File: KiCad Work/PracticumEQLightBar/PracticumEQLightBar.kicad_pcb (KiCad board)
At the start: 2 copper layers, 20 parts, among them U1 TEENSY 4.1, U2 TEENSY AUDIO ADAPTER BOARD RE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

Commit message: Updates to LED layout to match 49 key on schematic and PCB
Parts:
- removed the D8 at (104.8, 57.3)
- removed the D8 at (24.3, 57.4)
- removed the D8 at (137.0, 57.3)
- removed the D8 at (40.3, 57.3)
- removed the D8 at (72.7, 57.4)
- removed the D8 at (88.8, 57.3)
- removed the D8 at (121.0, 57.4)
- removed the D8 at (56.3, 57.3)
- removed the D8 at (153.0, 57.3)
- removed the D9 at (64.7, 57.5)
- removed the D9 at (129.0, 57.4)
- removed the D9 at (112.9, 57.5)
- removed the D9 at (48.3, 57.3)
- removed the D9 at (145.0, 57.3)
- removed the D9 at (16.2, 57.5)
- removed the D9 at (96.8, 57.3)
- removed the D9 at (32.3, 57.4)
- removed the D9 at (80.8, 57.4)
- added D1: APA102, LED_SMD:LED_RGB_5050-6, F.Cu at (61.0, 99.1)
- added D10: APA102, LED_SMD:LED_RGB_5050-6, F.Cu at (141.0, 99.1)
- added D11: APA102, LED_SMD:LED_RGB_5050-6, F.Cu at (149.9, 99.1)
- added D12: APA102, LED_SMD:LED_RGB_5050-6, F.Cu at (158.8, 99.1)
- added D13: APA102, LED_SMD:LED_RGB_5050-6, F.Cu at (167.6, 99.1)
- added D14: APA102, LED_SMD:LED_RGB_5050-6, F.Cu at (176.5, 99.1)
- added D15: APA102, LED_SMD:LED_RGB_5050-6, F.Cu at (185.4, 99.1)
- added D16: APA102, LED_SMD:LED_RGB_5050-6, F.Cu at (194.3, 99.1)
- added D17: APA102, LED_SMD:LED_RGB_5050-6, F.Cu at (203.2, 99.1)
- added D18: APA102, LED_SMD:LED_RGB_5050-6, F.Cu at (212.1, 99.1)
- added D19: APA102, LED_SMD:LED_RGB_5050-6, F.Cu at (221.0, 99.1)
- added D2: APA102, LED_SMD:LED_RGB_5050-6, F.Cu at (69.8, 99.1)
- added D20: APA102, LED_SMD:LED_RGB_5050-6, F.Cu at (229.9, 99.1)
- added D21: APA102, LED_SMD:LED_RGB_5050-6, F.Cu at (238.8, 99.1)
- added D22: APA102, LED_SMD:LED_RGB_5050-6, F.Cu at (247.7, 99.1)
- added D23: APA102, LED_SMD:LED_RGB_5050-6, F.Cu at (256.5, 99.1)
- added D24: APA102, LED_SMD:LED_RGB_5050-6, F.Cu at (265.4, 99.1)
- added D25: APA102, LED_SMD:LED_RGB_5050-6, F.Cu at (274.3, 99.1)
- added D26: APA102, LED_SMD:LED_RGB_5050-6, F.Cu at (283.2, 99.1)
- added D27: APA102, LED_SMD:LED_RGB_5050-6, F.Cu at (292.1, 99.1)
- added D28: APA102, LED_SMD:LED_RGB_5050-6, F.Cu at (301.0, 99.1)
- added D29: APA102, LED_SMD:LED_RGB_5050-6, F.Cu at (309.9, 99.1)
- added D3: APA102, LED_SMD:LED_RGB_5050-6, F.Cu at (78.7, 99.1)
- added D30: APA102, LED_SMD:LED_RGB_5050-6, F.Cu at (295.9, 90.2)
- added D31: APA102, LED_SMD:LED_RGB_5050-6, F.Cu at (287.0, 90.2)
- added D32: APA102, LED_SMD:LED_RGB_5050-6, F.Cu at (278.1, 90.2)
- added D33: APA102, LED_SMD:LED_RGB_5050-6, F.Cu at (260.4, 90.2)
- added D34: APA102, LED_SMD:LED_RGB_5050-6, F.Cu at (251.5, 90.2)
- added D35: APA102, LED_SMD:LED_RGB_5050-6, F.Cu at (233.7, 90.2)
- added D36: APA102, LED_SMD:LED_RGB_5050-6, F.Cu at (224.8, 90.2)
- added D37: APA102, LED_SMD:LED_RGB_5050-6, F.Cu at (215.9, 90.2)
- added D38: APA102, LED_SMD:LED_RGB_5050-6, F.Cu at (198.1, 90.2)
- added D39: APA102, LED_SMD:LED_RGB_5050-6, F.Cu at (189.2, 90.2)
- added D4: APA102, LED_SMD:LED_RGB_5050-6, F.Cu at (87.6, 99.1)
- added D40: APA102, LED_SMD:LED_RGB_5050-6, F.Cu at (171.4, 90.2)
- added D41: APA102, LED_SMD:LED_RGB_5050-6, F.Cu at (162.6, 90.2)
- added D42: APA102, LED_SMD:LED_RGB_5050-6, F.Cu at (153.7, 90.2)
- added D43: APA102, LED_SMD:LED_RGB_5050-6, F.Cu at (135.9, 90.2)
- added D44: APA102, LED_SMD:LED_RGB_5050-6, F.Cu at (127.0, 90.2)
- added D45: APA102, LED_SMD:LED_RGB_5050-6, F.Cu at (109.2, 90.2)
- added D46: APA102, LED_SMD:LED_RGB_5050-6, F.Cu at (100.3, 90.2)
- added D47: APA102, LED_SMD:LED_RGB_5050-6, F.Cu at (91.4, 90.2)
- added D48: APA102, LED_SMD:LED_RGB_5050-6, F.Cu at (73.7, 90.2)
- added D49: APA102, LED_SMD:LED_RGB_5050-6, F.Cu at (64.8, 90.2)
- added D5: APA102, LED_SMD:LED_RGB_5050-6, F.Cu at (96.5, 99.1)
- added D6: APA102, LED_SMD:LED_RGB_5050-6, F.Cu at (105.4, 99.1)
- added D7: APA102, LED_SMD:LED_RGB_5050-6, F.Cu at (114.3, 99.1)
- added D8: APA102, LED_SMD:LED_RGB_5050-6, F.Cu at (123.2, 99.1)
- added D9: APA102, LED_SMD:LED_RGB_5050-6, F.Cu at (132.1, 99.1)
- moved U1 106.9 mm to (68.6, 205.7)
- moved U2 48.2 mm to (111.8, 208.3)
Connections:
- U1 pad GND1: Net-(D8-GND) -> unconnected-(U1-GND-PadGND1)
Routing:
- net Net-(D1-VCC): track 0.00 -> 806.5 mm
- net Net-(D1-DI): track 0.00 -> 92.0 mm
- net Net-(D1-CI): track 0.00 -> 85.2 mm
- net Net-(D29-CO): track 0.00 -> 25.7 mm
- net Net-(D29-DO): track 0.00 -> 19.5 mm
- net Net-(D42-DO): track 0.00 -> 13.0 mm
- net Net-(D42-CO): track 0.00 -> 13.0 mm
- net Net-(D39-DO): track 0.00 -> 13.0 mm
- net Net-(D39-CO): track 0.00 -> 13.0 mm
- net Net-(D32-DO): track 0.00 -> 13.0 mm
- net Net-(D32-CO): track 0.00 -> 13.0 mm
- net Net-(D47-DO): track 0.00 -> 13.0 mm
- net Net-(D47-CO): track 0.00 -> 13.0 mm
- net Net-(D44-DO): track 0.00 -> 13.0 mm
- net Net-(D44-CO): track 0.00 -> 13.0 mm
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- added copper zone on B.Cu, net (none)
- added copper zone on F.Cu, net (none)
- added copper zone on B.Cu, net GND
- added copper zone on F.Cu, net GND
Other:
- board outline added: 300 x 300 mm

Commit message: Completed preliminary schematic
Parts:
- moved U2 48.2 mm to (66.0, 192.9), turned to -90 degrees
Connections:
- D1 pad 1: Net-(D1-DI) -> unconnected-(D1-DI-Pad1)
- D1 pad 2: Net-(D1-CI) -> unconnected-(D1-CI-Pad2)
- D45 pad 1: Net-(D44-DO) -> Net-(D45-DI)
- D45 pad 2: Net-(D44-CO) -> Net-(D45-CI)
- D7 pad 5: Net-(D7-CO) -> Net-(D45-CI)
- D7 pad 6: Net-(D7-DO) -> Net-(D45-DI)
- U1 pad 0: Net-(D1-CI) -> Net-(U1-RX1)
- U1 pad 1: Net-(D1-DI) -> Net-(U1-TX1)
- U1 pad 10: unconnected-(U1-CS1-Pad10) -> Net-(U1-CS1)
- U1 pad 11: unconnected-(U1-MOSI-Pad11) -> Net-(U1-MOSI)
- U1 pad 12: unconnected-(U1-MISO-Pad12) -> Net-(U1-MISO)
- U1 pad 13: unconnected-(U1-SCK-Pad13) -> Net-(U1-SCK)
- U1 pad 14: unconnected-(U1-A0-Pad14) -> Net-(U1-A0)
- U1 pad 15: unconnected-(U1-A1-Pad15) -> Net-(U1-A1)
- U1 pad 16: unconnected-(U1-A2-Pad16) -> Net-(U1-A2)
- U1 pad 17: unconnected-(U1-A3-Pad17) -> Net-(U1-A3)
- U1 pad 18: unconnected-(U1-A4-Pad18) -> Net-(U1-A4)
- U1 pad 19: unconnected-(U1-A5-Pad19) -> Net-(U1-A5)
- U1 pad 2: unconnected-(U1-OUT2-Pad2) -> Net-(U1-OUT2)
- U1 pad 20: unconnected-(U1-A6-Pad20) -> Net-(U1-A6)
- U1 pad 21: unconnected-(U1-A7-Pad21) -> Net-(U1-A7)
- U1 pad 22: unconnected-(U1-A8-Pad22) -> Net-(U1-A8)
- U1 pad 23: unconnected-(U1-A9-Pad23) -> Net-(U1-A9)
- U1 pad 3: unconnected-(U1-LRCLK2-Pad3) -> Net-(U1-LRCLK2)
- U1 pad 3.3V_2: unconnected-(U1-3.3V__1-Pad3.3V_2) -> Net-(U1-3.3V__1)
- U1 pad 4: unconnected-(U1-BCLK2-Pad4) -> Net-(U1-BCLK2)
- U1 pad 5: unconnected-(U1-IN2-Pad5) -> Net-(U1-IN2)
- U1 pad 5V: Net-(D1-VCC) -> unconnected-(U1-Pad5V)
- U1 pad 6: unconnected-(U1-OUT1D-Pad6) -> Net-(U1-OUT1D)
- U1 pad 7: unconnected-(U1-RX2-Pad7) -> Net-(U1-RX2)
- U1 pad 8: unconnected-(U1-TX2-Pad8) -> Net-(U1-TX2)
- U1 pad 9: unconnected-(U1-OUT1C-Pad9) -> Net-(U1-OUT1C)
- U1 pad GND1: unconnected-(U1-GND-PadGND1) -> Net-(U1-GND)
- U1 pad GND3: unconnected-(U1-GND__2-PadGND3) -> Net-(U1-GND__2)
- U1 pad VIN: unconnected-(U1-PadVIN) -> Net-(U1-PadVIN)
- U2 pad 0: unconnected-(U2-Pad0) -> Net-(U1-RX1)
- U2 pad 1: unconnected-(U2-Pad1) -> Net-(U1-TX1)
- U2 pad 10: unconnected-(U2-SDCS-Pad10) -> Net-(U1-CS1)
- U2 pad 11: unconnected-(U2-MOSI-Pad11) -> Net-(U1-MOSI)
- U2 pad 12: unconnected-(U2-MISO-Pad12) -> Net-(U1-MISO)
- U2 pad 13: unconnected-(U2-SCK-Pad13) -> Net-(U1-SCK)
- U2 pad 14: unconnected-(U2-Pad14) -> Net-(U1-A0)
- U2 pad 15: unconnected-(U2-VOL15_A1-Pad15) -> Net-(U1-A1)
- U2 pad 16: unconnected-(U2-Pad16) -> Net-(U1-A2)
- U2 pad 17: unconnected-(U2-Pad17) -> Net-(U1-A3)
- U2 pad 18: unconnected-(U2-SDA-Pad18) -> Net-(U1-A4)
- U2 pad 19: unconnected-(U2-SCL-Pad19) -> Net-(U1-A5)
- U2 pad 2: unconnected-(U2-Pad2) -> Net-(U1-OUT2)
- U2 pad 20: unconnected-(U2-LRCLK1-Pad20) -> Net-(U1-A6)
- U2 pad 21: unconnected-(U2-BCLK1-Pad21) -> Net-(U1-A7)
- U2 pad 22: unconnected-(U2-Pad22) -> Net-(U1-A8)
- U2 pad 23: unconnected-(U2-MCLK1-Pad23) -> Net-(U1-A9)
- U2 pad 3: unconnected-(U2-Pad3) -> Net-(U1-LRCLK2)
- U2 pad 3V: unconnected-(U2-Pad3V) -> Net-(U1-3.3V__1)
- U2 pad 4: unconnected-(U2-Pad4) -> Net-(U1-BCLK2)
- U2 pad 5: unconnected-(U2-Pad5) -> Net-(U1-IN2)
- U2 pad 5V: unconnected-(U2-Pad5V) -> Net-(U1-PadVIN)
- U2 pad 6: unconnected-(U2-MEMCS-Pad6) -> Net-(U1-OUT1D)
- U2 pad 7: unconnected-(U2-OUT1A-Pad7) -> Net-(U1-RX2)
- U2 pad 8: unconnected-(U2-IN1-Pad8) -> Net-(U1-TX2)
- U2 pad 9: unconnected-(U2-Pad9) -> Net-(U1-OUT1C)
- U2 pad G: unconnected-(U2-PadG) -> Net-(U1-GND__2)
- U2 pad GND: unconnected-(U2-PadGND) -> Net-(U1-GND)
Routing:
- net (no net): track 0.00 -> 177.2 mm
- net Net-(D1-DI): track 92.0 -> 0.00 mm
- net Net-(D1-CI): track 85.2 -> 0.00 mm

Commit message: Schematic and PCB updated to show all 49 LEDs
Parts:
- moved D1 166.1 mm to (78.7, 264.2)
- moved D10 166.1 mm to (158.8, 264.2)
- moved D11 166.1 mm to (167.6, 264.2)
- moved D12 166.1 mm to (176.5, 264.2)
- moved D13 166.1 mm to (185.4, 264.2)
- moved D14 166.1 mm to (194.3, 264.2)
- moved D15 166.1 mm to (203.2, 264.2)
- moved D16 166.1 mm to (212.1, 264.2)
- moved D17 166.1 mm to (221.0, 264.2)
- moved D18 166.1 mm to (229.9, 264.2)
- moved D19 166.1 mm to (238.8, 264.2)
- moved D2 166.1 mm to (87.6, 264.2)
- moved D20 166.1 mm to (247.7, 264.2)
- moved D21 166.1 mm to (256.5, 264.2)
- moved D22 166.1 mm to (265.4, 264.2)
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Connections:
- D1 pad 1: unconnected-(D1-DI-Pad1) -> Net-(D1-DI)
- D1 pad 2: unconnected-(D1-CI-Pad2) -> Net-(D1-CI)
- D1 pad 4: Net-(D1-VCC) -> 5V USB
- D10 pad 4: Net-(D1-VCC) -> 5V USB
- D11 pad 4: Net-(D1-VCC) -> 5V USB
- D12 pad 4: Net-(D1-VCC) -> 5V USB
- D13 pad 4: Net-(D1-VCC) -> 5V USB
- D14 pad 4: Net-(D1-VCC) -> 5V USB
- D15 pad 4: Net-(D1-VCC) -> 5V USB
- D16 pad 4: Net-(D1-VCC) -> 5V USB
- D17 pad 4: Net-(D1-VCC) -> 5V USB
- D18 pad 4: Net-(D1-VCC) -> 5V USB
- D19 pad 4: Net-(D1-VCC) -> 5V USB
- D2 pad 4: Net-(D1-VCC) -> 5V USB
- D20 pad 4: Net-(D1-VCC) -> 5V USB
- D21 pad 4: Net-(D1-VCC) -> 5V USB
- D22 pad 4: Net-(D1-VCC) -> 5V USB
- D23 pad 4: Net-(D1-VCC) -> 5V USB
- D24 pad 4: Net-(D1-VCC) -> 5V USB
- D25 pad 4: Net-(D1-VCC) -> 5V USB
- D26 pad 4: Net-(D1-VCC) -> 5V USB
- D27 pad 4: Net-(D1-VCC) -> 5V USB
- D28 pad 4: Net-(D1-VCC) -> 5V USB
- D29 pad 4: Net-(D1-VCC) -> 5V USB
- D3 pad 4: Net-(D1-VCC) -> 5V USB
- D30 pad 4: Net-(D1-VCC) -> 5V USB
- D31 pad 4: Net-(D1-VCC) -> 5V USB
- D32 pad 4: Net-(D1-VCC) -> 5V USB
- D33 pad 4: Net-(D1-VCC) -> 5V USB
- D34 pad 4: Net-(D1-VCC) -> 5V USB
- D35 pad 4: Net-(D1-VCC) -> 5V USB
- D36 pad 4: Net-(D1-VCC) -> 5V USB
- D37 pad 4: Net-(D1-VCC) -> 5V USB
- D38 pad 4: Net-(D1-VCC) -> 5V USB
- D39 pad 4: Net-(D1-VCC) -> 5V USB
- D4 pad 4: Net-(D1-VCC) -> 5V USB
- D40 pad 4: Net-(D1-VCC) -> 5V USB
- D41 pad 4: Net-(D1-VCC) -> 5V USB
- D42 pad 4: Net-(D1-VCC) -> 5V USB
- D43 pad 4: Net-(D1-VCC) -> 5V USB
- D44 pad 4: Net-(D1-VCC) -> 5V USB
- D45 pad 1: Net-(D45-DI) -> Net-(D44-DO)
- D45 pad 2: Net-(D45-CI) -> Net-(D44-CO)
- D45 pad 4: Net-(D1-VCC) -> 5V USB
- D46 pad 4: Net-(D1-VCC) -> 5V USB
- D47 pad 4: Net-(D1-VCC) -> 5V USB
- D48 pad 4: Net-(D1-VCC) -> 5V USB
- D49 pad 4: Net-(D1-VCC) -> 5V USB
- D5 pad 4: Net-(D1-VCC) -> 5V USB
- D6 pad 4: Net-(D1-VCC) -> 5V USB
- D7 pad 4: Net-(D1-VCC) -> 5V USB
- D7 pad 5: Net-(D45-CI) -> Net-(D7-CO)
- D7 pad 6: Net-(D45-DI) -> Net-(D7-DO)
- D8 pad 4: Net-(D1-VCC) -> 5V USB
- D9 pad 4: Net-(D1-VCC) -> 5V USB
- U1 pad 24: unconnected-(U1-A10-Pad24) -> Net-(D1-CI)
- U1 pad 25: unconnected-(U1-A11-Pad25) -> Net-(D1-DI)
- U1 pad VIN: Net-(U1-PadVIN) -> 5V USB
- U2 pad 5V: Net-(U1-PadVIN) -> 5V USB
- U2 pad GND_MIC: unconnected-(U2-MIC_GND-PadGND_MIC) -> Net-(MK1--)
- U2 pad INGND1: unconnected-(U2-PadINGND1) -> Net-(J1-PadS)
- U2 pad INGND2: unconnected-(U2-PadINGND2) -> Net-(J1-PadS)
- U2 pad INL: unconnected-(U2-PadINL) -> Net-(J1-PadT)
- U2 pad INR: unconnected-(U2-PadINR) -> Net-(J1-PadR)
- U2 pad MIC: unconnected-(U2-PadMIC) -> Net-(MK1-+)
- U2 pad VOL: unconnected-(U2-PadVOL) -> Net-(RV1-Pad2)
- U2 pad VOL_3.3V: unconnected-(U2-PadVOL_3.3V) -> Net-(RV1-Pad1)
- U2 pad VOL_GND: unconnected-(U2-PadVOL_GND) -> Net-(RV1-Pad3)
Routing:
- net Net-(D1-VCC): track 806.5 -> 0.00 mm
- net (no net): track 177.2 -> 0.00 mm
- net Net-(D1-CI): track 0.00 -> 78.9 mm
- net Net-(D1-DI): track 0.00 -> 72.1 mm
- net Net-(D29-DO): track 19.5 -> 24.8 mm
- net Net-(D29-CO): track 25.7 -> 30.8 mm

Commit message: Resized edge cuts and updated titleblocks
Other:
- board size 300 x 300 mm -> 300 x 114.6 mm
- board text added: "~49 keys, mirrored in light~"
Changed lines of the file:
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@@
 	)
 	(paper "A2")
+	(title_block
+		(title "EchoKeys 49")
+		(date "2025-11-08")
+		(rev "1")
+		(company "Team 3, ECE 411, Fall 2025, Portland State University")
+	)
 	(layers
 		(0 "F.Cu" signal)
@@
 		(tenting front back)
 		(pcbplotparams
-			(layerselection 0x00000000_00000000_55555555_5755f5ff)
+			(layerselection 0x00000000_00000000_55555555_5755f5fa)
 			(plot_on_all_layers_selection 0x00000000_00000000_00000000_00000000)
 			(disableapertmacros no)
@@
 			(crossoutdnponfab yes)
 			(subtractmaskfromsilk no)
-			(outputformat 1)
+			(outputformat 4)
 			(mirror no)
-			(drillshape 1)
+			(drillshape 0)
 			(scaleselection 1)
 			(outputdirectory "")
@@
 	)
 	(gr_rect
-		(start 45 45)
-		(end 345 345)
+		(start 45 166.92)
+		(end 345 281.5)
 		(stroke
 			(width 0.05)
@@
 		(layer "Edge.Cuts")
 	)
+	(gr_text "~49 keys, mirrored in light~"
+		(at 114.3 222.25 0)
+		(layer "F.SilkS")
+		(effects
+			(font
+				(size 1 1)
+				(thickness 0.125)
+				(italic yes)
+			)
+			(justify left bottom)
+		)
+	)
 	(segment

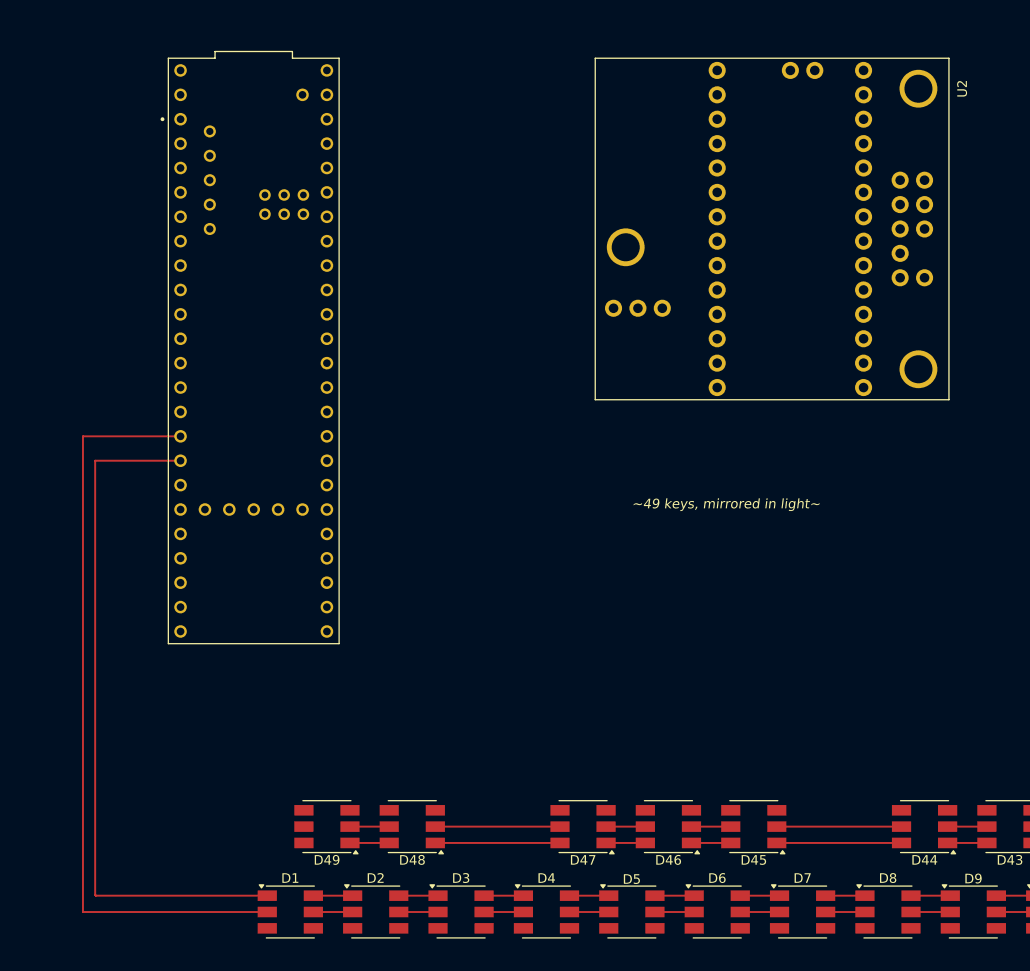
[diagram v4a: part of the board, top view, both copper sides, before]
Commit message: Added SN74 logic level shifter to schematic and PCB
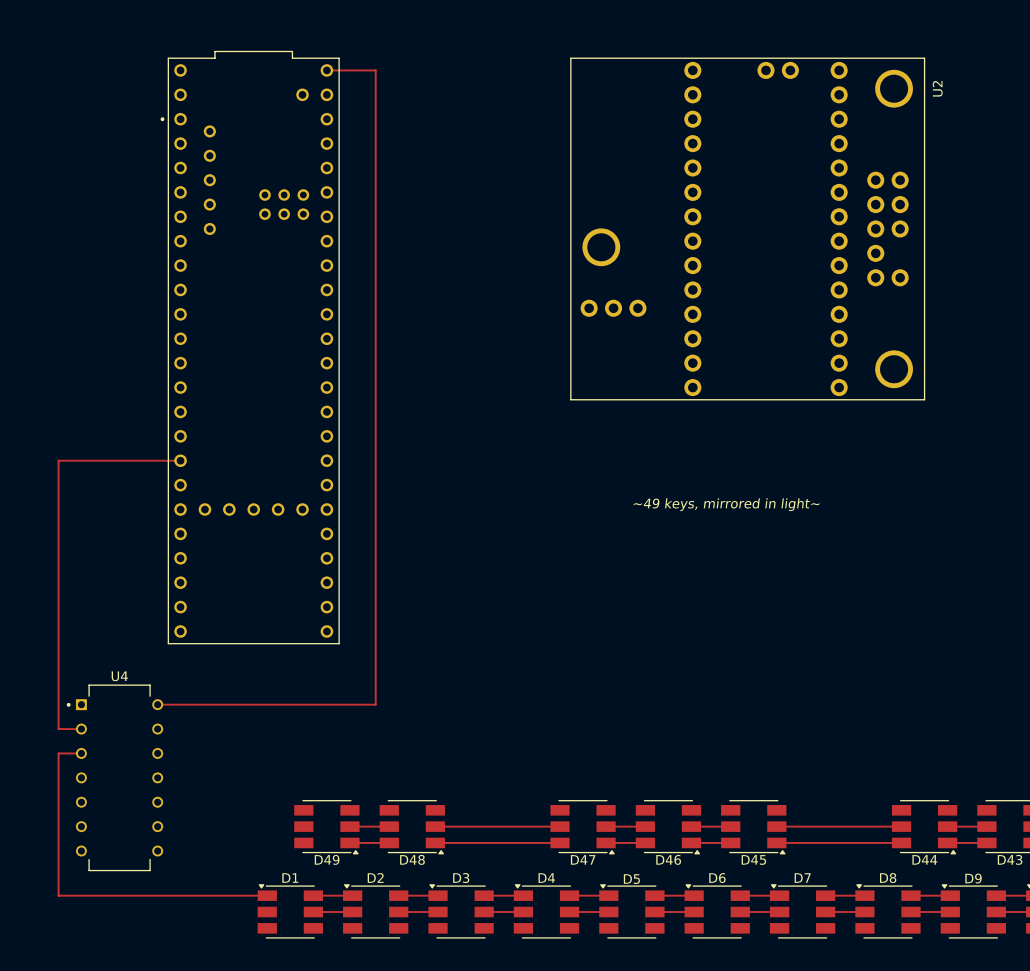
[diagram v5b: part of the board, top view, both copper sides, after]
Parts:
- added U4: SN74AHCT125N, SN74AHCT125N:DIP794W45P254L1930H508Q14, F.Cu at (61.0, 250.2)
- moved U2 2.54 mm to (125.7, 193.0)
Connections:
- D1 pad 1: Net-(D1-DI) -> /5.0V DATA
- D1 pad 2: Net-(D1-CI) -> unconnected-(D1-CI-Pad2)
- D1 pad 4: 5V USB -> Net-(D1-VCC)
- D10 pad 4: 5V USB -> Net-(D1-VCC)
- D11 pad 4: 5V USB -> Net-(D1-VCC)
- D12 pad 4: 5V USB -> Net-(D1-VCC)
- D13 pad 4: 5V USB -> Net-(D1-VCC)
- D14 pad 4: 5V USB -> Net-(D1-VCC)
- D15 pad 4: 5V USB -> Net-(D1-VCC)
- D16 pad 4: 5V USB -> Net-(D1-VCC)
- D17 pad 4: 5V USB -> Net-(D1-VCC)
- D18 pad 4: 5V USB -> Net-(D1-VCC)
- D19 pad 4: 5V USB -> Net-(D1-VCC)
- D2 pad 4: 5V USB -> Net-(D1-VCC)
- D20 pad 4: 5V USB -> Net-(D1-VCC)
- D21 pad 4: 5V USB -> Net-(D1-VCC)
- D22 pad 4: 5V USB -> Net-(D1-VCC)
- D23 pad 4: 5V USB -> Net-(D1-VCC)
- D24 pad 4: 5V USB -> Net-(D1-VCC)
- D25 pad 4: 5V USB -> Net-(D1-VCC)
- D26 pad 4: 5V USB -> Net-(D1-VCC)
- D27 pad 4: 5V USB -> Net-(D1-VCC)
- D28 pad 4: 5V USB -> Net-(D1-VCC)
- D29 pad 4: 5V USB -> Net-(D1-VCC)
- D3 pad 4: 5V USB -> Net-(D1-VCC)
- D30 pad 4: 5V USB -> Net-(D1-VCC)
- D31 pad 4: 5V USB -> Net-(D1-VCC)
- D32 pad 4: 5V USB -> Net-(D1-VCC)
- D33 pad 4: 5V USB -> Net-(D1-VCC)
- D34 pad 4: 5V USB -> Net-(D1-VCC)
- D35 pad 4: 5V USB -> Net-(D1-VCC)
- D36 pad 4: 5V USB -> Net-(D1-VCC)
- D37 pad 4: 5V USB -> Net-(D1-VCC)
- D38 pad 4: 5V USB -> Net-(D1-VCC)
- D39 pad 4: 5V USB -> Net-(D1-VCC)
- D4 pad 4: 5V USB -> Net-(D1-VCC)
- D40 pad 4: 5V USB -> Net-(D1-VCC)
- D41 pad 4: 5V USB -> Net-(D1-VCC)
- D42 pad 4: 5V USB -> Net-(D1-VCC)
- D43 pad 4: 5V USB -> Net-(D1-VCC)
- D44 pad 4: 5V USB -> Net-(D1-VCC)
- D45 pad 4: 5V USB -> Net-(D1-VCC)
- D46 pad 4: 5V USB -> Net-(D1-VCC)
- D47 pad 4: 5V USB -> Net-(D1-VCC)
- D48 pad 4: 5V USB -> Net-(D1-VCC)
- D49 pad 4: 5V USB -> Net-(D1-VCC)
- D5 pad 4: 5V USB -> Net-(D1-VCC)
- D6 pad 4: 5V USB -> Net-(D1-VCC)
- D7 pad 4: 5V USB -> Net-(D1-VCC)
- D8 pad 4: 5V USB -> Net-(D1-VCC)
- D9 pad 4: 5V USB -> Net-(D1-VCC)
- U1 pad 24: Net-(D1-CI) -> unconnected-(U1-A10-Pad24)
- U1 pad 25: Net-(D1-DI) -> /3.3V DATA
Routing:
- net 5V USB: track 0.00 -> 93.8 mm
- net Net-(D1-CI): track 78.9 -> 0.00 mm
- net Net-(D1-DI): track 72.1 -> 0.00 mm
- net /3.3V DATA: track 0.00 -> 43.0 mm
- net /5.0V DATA: track 0.00 -> 39.1 mm

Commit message: Updated rev 1.1 drawing sheet PDFs
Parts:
- moved D1 132.8 mm to (61.8, 132.4)
- moved D10 132.8 mm to (141.8, 132.4)
- moved D11 132.8 mm to (150.7, 132.4)
- moved D12 132.8 mm to (159.6, 132.4)
- moved D13 132.8 mm to (168.5, 132.4)
- moved D14 132.8 mm to (177.4, 132.4)
- moved D15 132.8 mm to (186.3, 132.4)
- moved D16 132.8 mm to (195.2, 132.4)
- moved D17 132.8 mm to (204.1, 132.4)
- moved D18 132.8 mm to (212.9, 132.4)
- moved D19 132.8 mm to (221.8, 132.4)
- moved D2 132.8 mm to (70.7, 132.4)
- moved D20 132.8 mm to (230.7, 132.4)
- moved D21 132.8 mm to (239.6, 132.4)
- moved D22 132.8 mm to (248.5, 132.4)
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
